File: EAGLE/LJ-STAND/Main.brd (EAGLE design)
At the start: 158.5 x 133.6 mm, 130 parts

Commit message: PCB design errors
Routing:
- net LS14: track 123.5 -> 126.4 mm
- net SCL: track 257.1 -> 259.8 mm
- net +3V3: track 463.8 -> 465.7 mm
- net N$35: track 33.1 -> 35.0 mm
- net SDA: track 284.5 -> 282.7 mm, vias 12 -> 14
- net MOSI: track 224.9 -> 226.4 mm
- net LS15: track 66.5 -> 67.5 mm
- net LS7: track 9.68 -> 10.6 mm
- net LED5: track 67.7 -> 68.4 mm

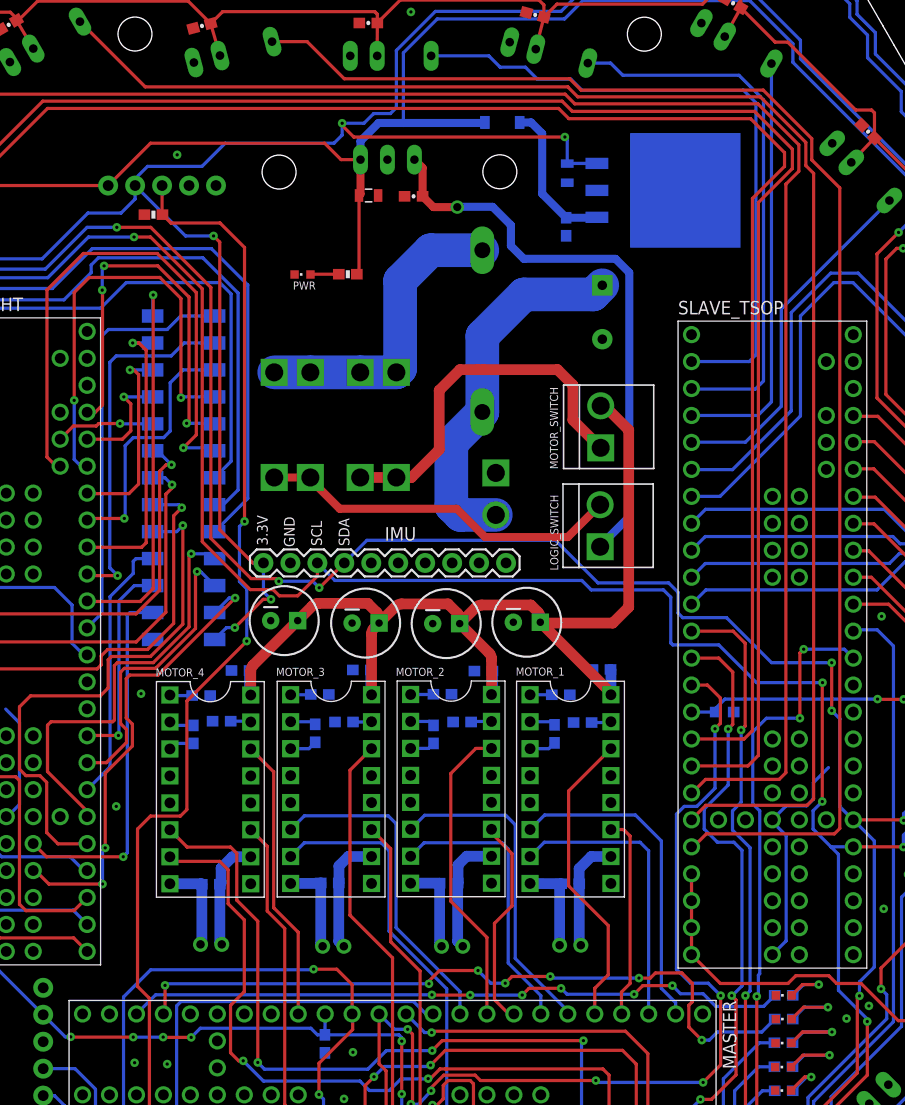
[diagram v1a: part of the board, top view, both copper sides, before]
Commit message: bigger motor traces
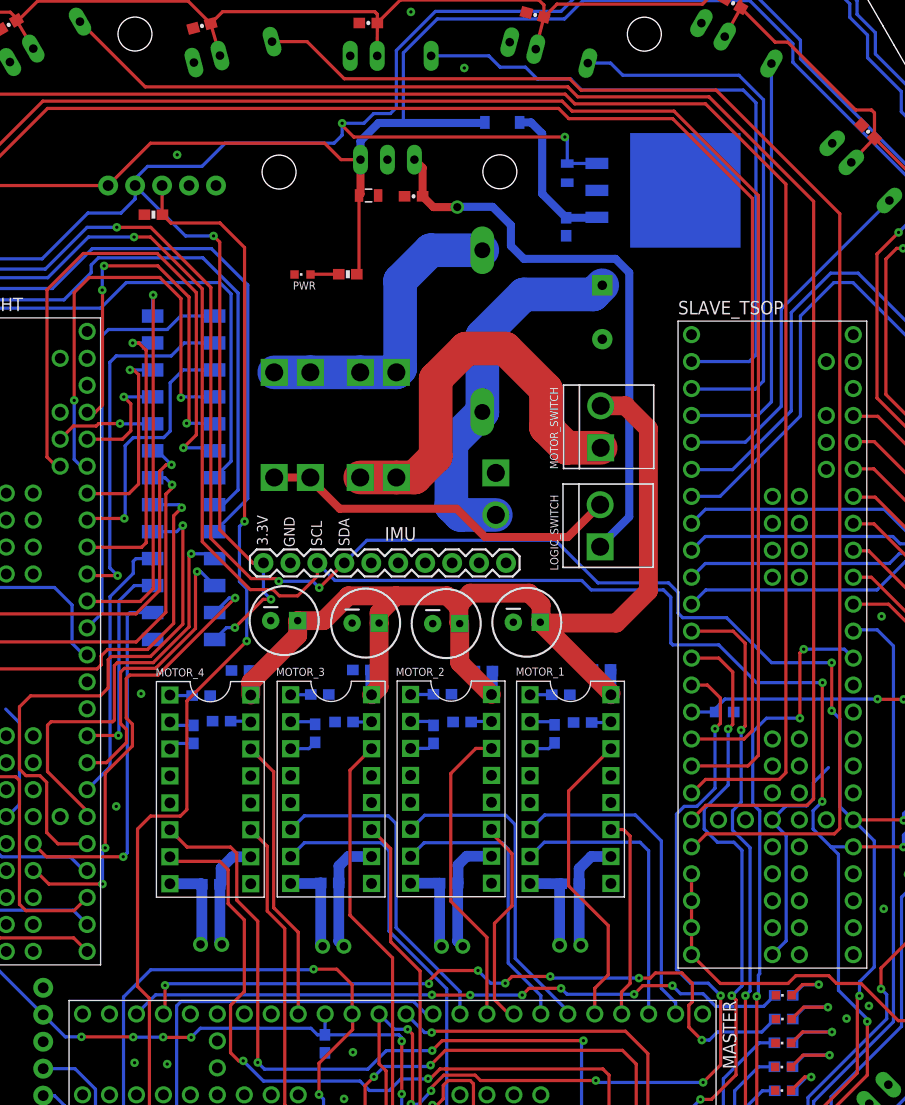
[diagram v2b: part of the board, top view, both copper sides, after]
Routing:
- net TSOP20: track 162.4 -> 155.3 mm
- net MOTOR_PWR: track 100.1 -> 107.0 mm
- net TSOP19: track 176.1 -> 169.3 mm
- net TSOP21: track 153.4 -> 149.5 mm
- net TSOP22: track 147.6 -> 144.8 mm
- net N$21: track 35.1 -> 37.9 mm
- net TSOP23: track 135.4 -> 132.8 mm
- net GND: vias 20 -> 21

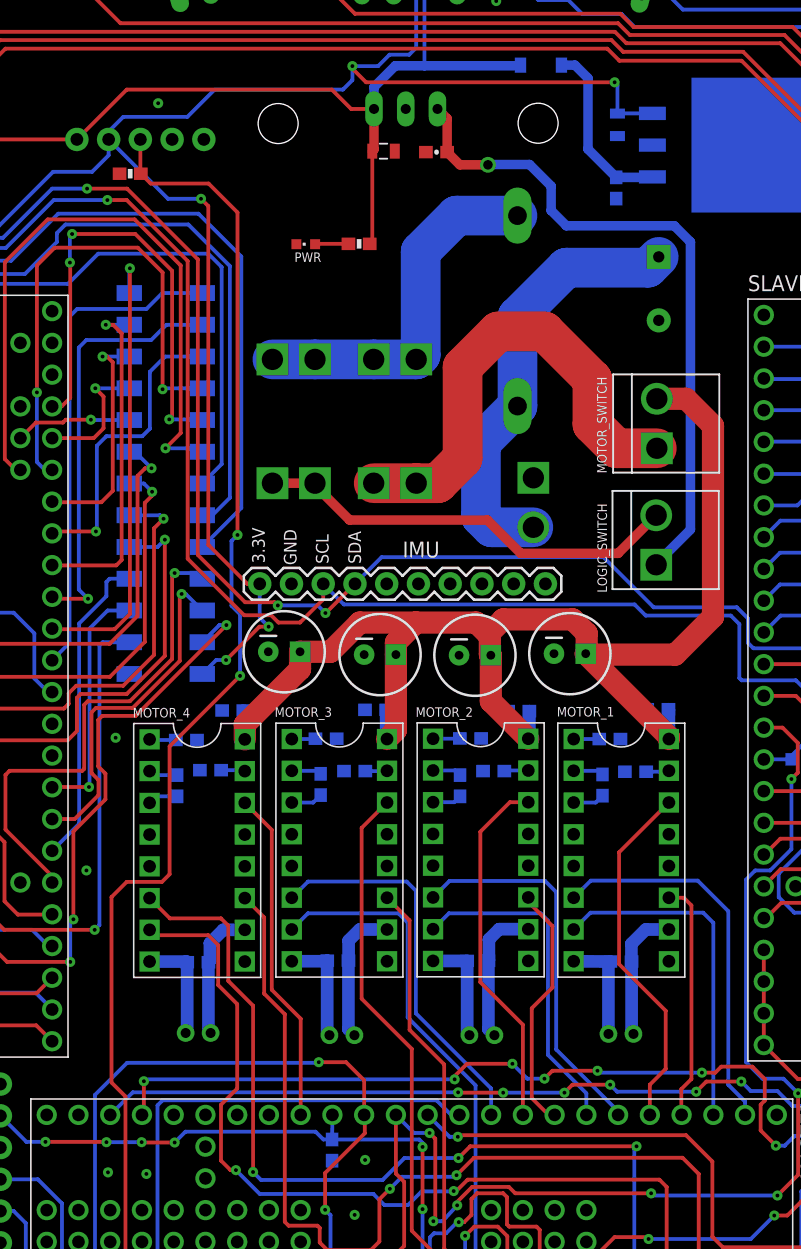
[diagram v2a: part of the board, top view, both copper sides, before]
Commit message: Light sensor PCB error fixing
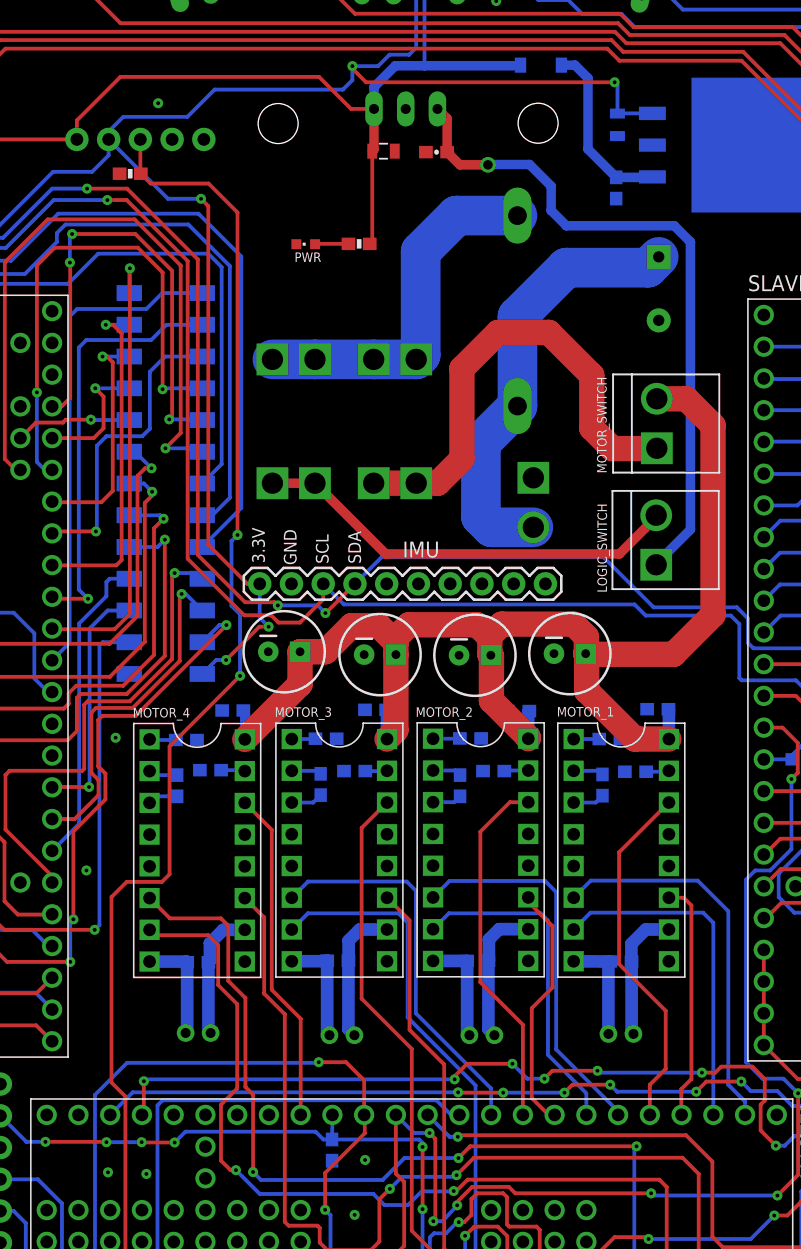
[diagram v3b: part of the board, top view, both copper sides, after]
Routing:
- net +5V: track 257.1 -> 258.9 mm

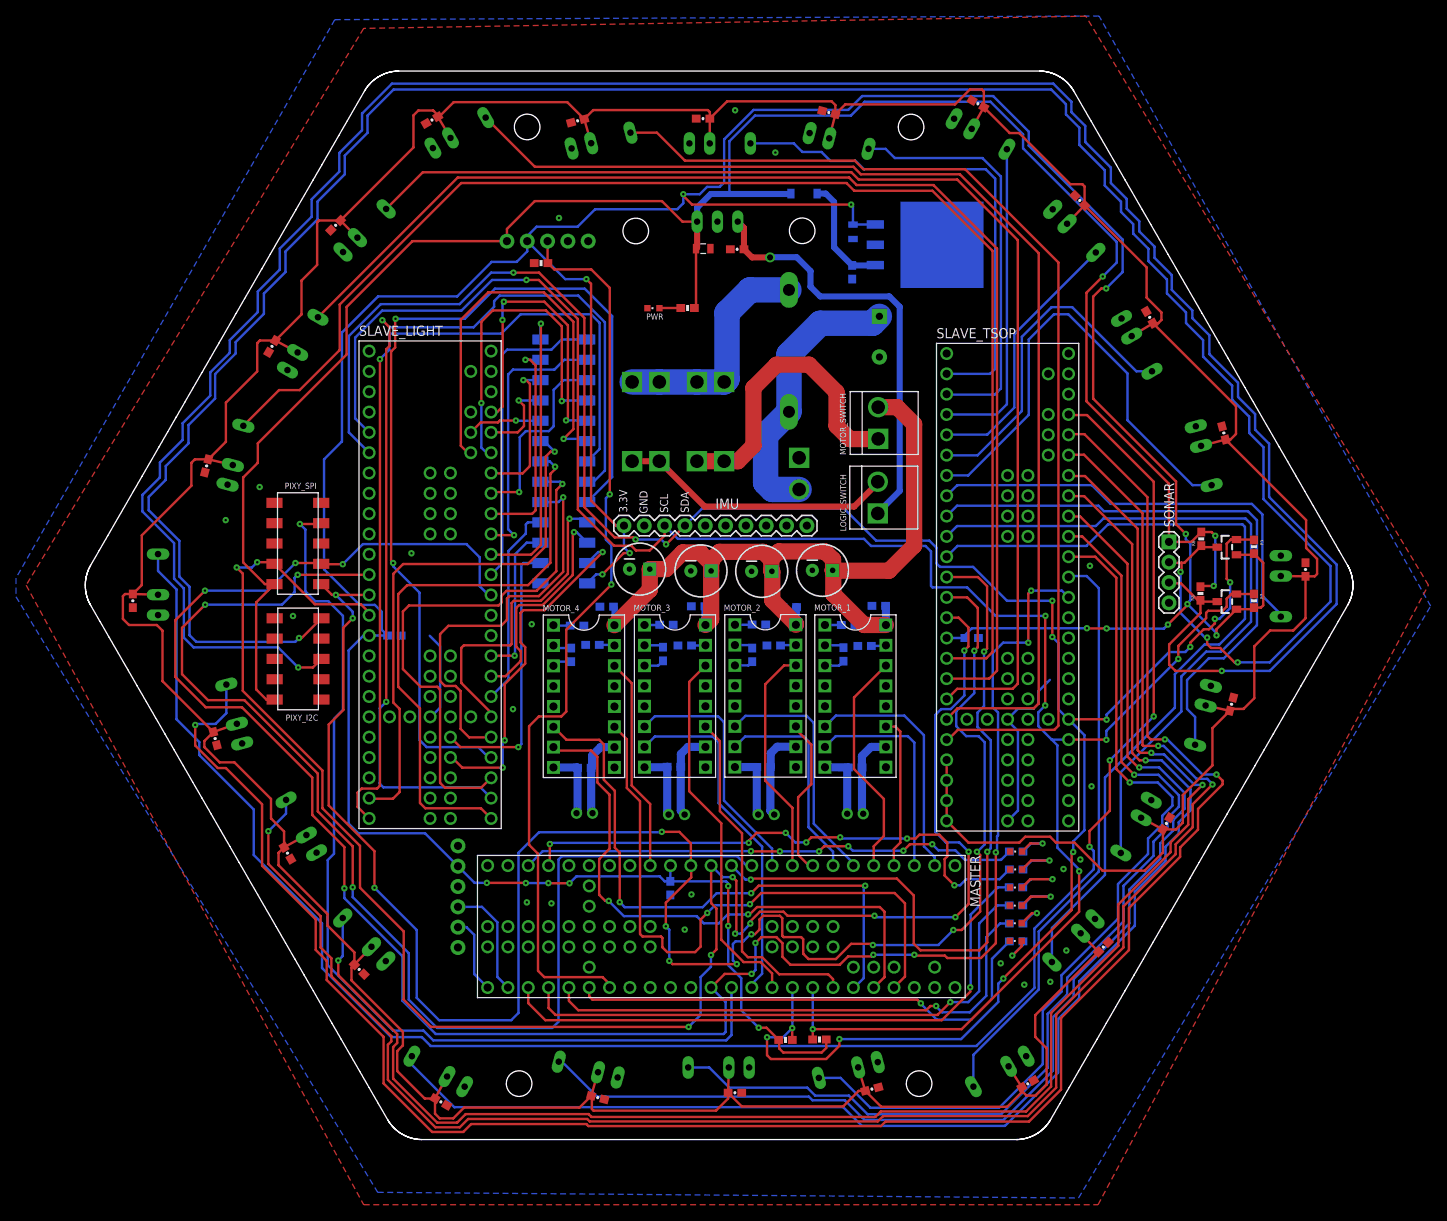
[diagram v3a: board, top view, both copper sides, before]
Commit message: Main pcb check against dimensions, made text bigger on both pcbs
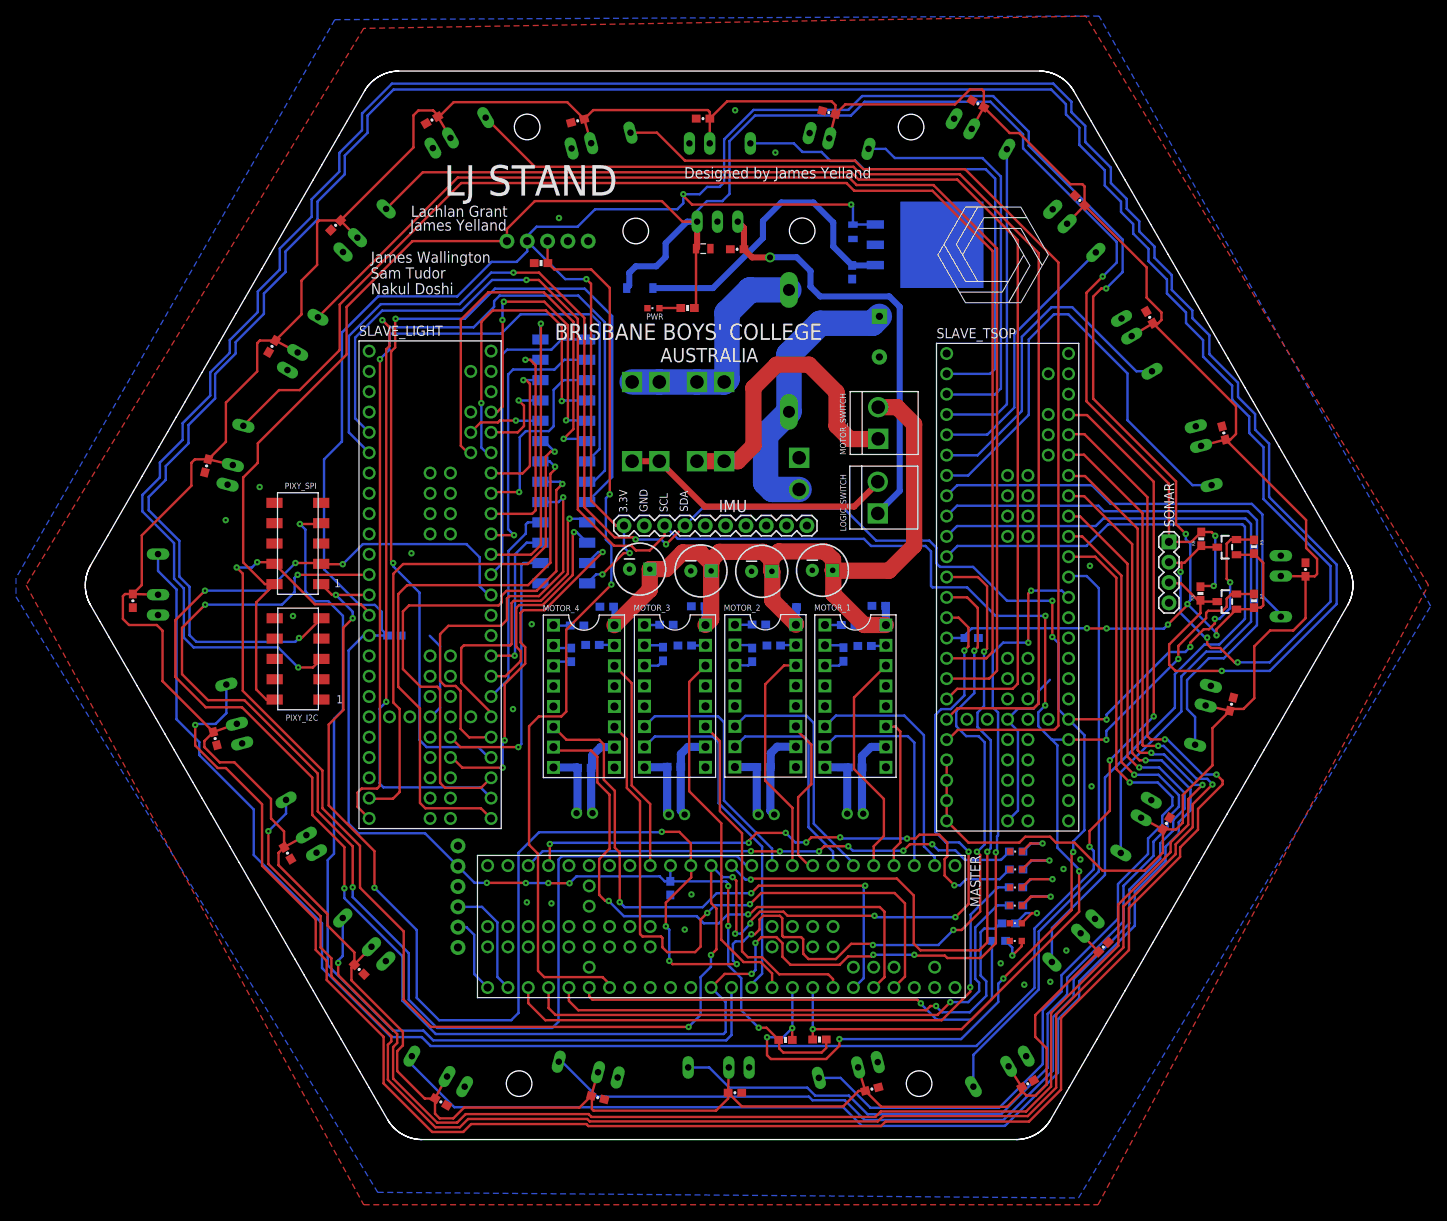
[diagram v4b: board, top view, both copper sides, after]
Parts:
- moved D2 23.7 mm to (138.8, 144.8)
- moved R18 2.17 mm to (183.7, 63.2)
- moved R19 0.93 mm to (184.9, 65.4)
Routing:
- net N$36: track 14.3 -> 38.5 mm
- net +5V: track 258.9 -> 265.1 mm
- net N$23: track 4.70 -> 5.62 mm
- net LED1: track 61.9 -> 61.0 mm
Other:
- board text added: "AUSTRALIA"
- board text added: "BRISBANE BOYS' COLLEGE"
- board text added: "Designed by James Yelland"
- board text added: "James Wallington"
- board text added: "James Yelland"
- board text added: "LJ STAND"
- board text added: "Lachlan Grant"
- board text added: "Nakul Doshi"
- board text added: "Sam Tudor"

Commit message: PCB finalising
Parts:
- C11, C13: device SparkFun-Capacitors:0603-CAP -> SparkFun-Capacitors:0805
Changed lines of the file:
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@@
 <setting verticaltext="up"/>
 </settings>
-<grid distance="1" unitdist="mil" unit="mil" style="lines" multiple="1" display="yes" altdistance="1" altunitdist="mil" altunit="mil"/>
+<grid distance="1" unitdist="mil" unit="mm" style="lines" multiple="1" display="yes" altdistance="1" altunitdist="mil" altunit="mil"/>
 <layers>
 <layer number="1" name="Top" color="4" fill="1" visible="yes" active="yes"/>
@@
 <attribute name="VALUE" x="213.591490625" y="91.4835875" size="0.4064" layer="27" font="vector" rot="R75"/>
 </element>
-<element name="C11" library="SparkFun-Capacitors" package="0603-CAP" value="10uF" x="150.9522" y="149.6314" smashed="yes" rot="R180">
+<element name="C11" library="SparkFun-Capacitors" package="0805" value="10uF" x="150.9522" y="149.6314" smashed="yes" rot="R180">
 <attribute name="VALUE" x="151.0284" y="148.5392" size="0.4064" layer="27" font="vector" rot="R180"/>
 </element>
@@
 <attribute name="VALUE" x="145.8214" y="148.2852" size="0.4064" layer="27" font="vector"/>
 </element>
-<element name="C13" library="SparkFun-Capacitors" package="0603-CAP" value="10uF" x="165.3286" y="146.7612" smashed="yes" rot="MR270">
+<element name="C13" library="SparkFun-Capacitors" package="0805" value="10uF" x="165.3286" y="146.7612" smashed="yes" rot="MR270">
 <attribute name="VALUE" x="166.4716" y="147.7772" size="0.4064" layer="28" font="vector" rot="MR270"/>
 </element>
@@
 <via x="155.067" y="148.6154" extent="1-16" drill="0.762"/>
 <wire x1="155.067" y1="148.6154" x2="152.8182" y2="148.6154" width="0.762" layer="1"/>
-<wire x1="152.8182" y1="148.6154" x2="151.8022" y2="149.6314" width="0.762" layer="1"/>
-<wire x1="151.8022" y1="149.6314" x2="151.8022" y2="152.312" width="0.762" layer="1"/>
+<wire x1="152.8182" y1="148.6154" x2="151.8522" y2="149.6314" width="0.762" layer="1"/>
+<wire x1="151.8522" y1="149.6314" x2="151.8022" y2="152.312" width="0.762" layer="1"/>
 <wire x1="151.8022" y1="152.312" x2="151.0284" y2="153.0858" width="0.762" layer="1"/>
 </signal>
@@
 <contactref element="C13" pad="1"/>
 <contactref element="VREG-3.3V" pad="1"/>
-<wire x1="165.3286" y1="147.6112" x2="168.1852" y2="147.6112" width="0.762" layer="16"/>
+<wire x1="165.3286" y1="147.6612" x2="168.1852" y2="147.6112" width="0.762" layer="16"/>
 <wire x1="168.1852" y1="147.6112" x2="168.2242" y2="147.6502" width="0.762" layer="16"/>
 <wire x1="140.4231" y1="144.78" x2="147.9296" y2="144.78" width="0.762" layer="16"/>
@@
 <wire x1="160.4772" y1="155.4734" x2="162.9664" y2="152.9842" width="0.762" layer="16"/>
 <wire x1="162.9664" y1="152.9842" x2="162.9664" y2="149.9734" width="0.762" layer="16"/>
-<wire x1="162.9664" y1="149.9734" x2="165.3286" y2="147.6112" width="0.762" layer="16"/>
+<wire x1="162.9664" y1="149.9734" x2="165.3286" y2="147.6612" width="0.762" layer="16"/>
 </signal>
 <signal name="PWR">
